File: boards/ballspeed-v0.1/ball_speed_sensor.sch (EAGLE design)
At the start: 7 parts, among them U1 MPM3620GQV-P

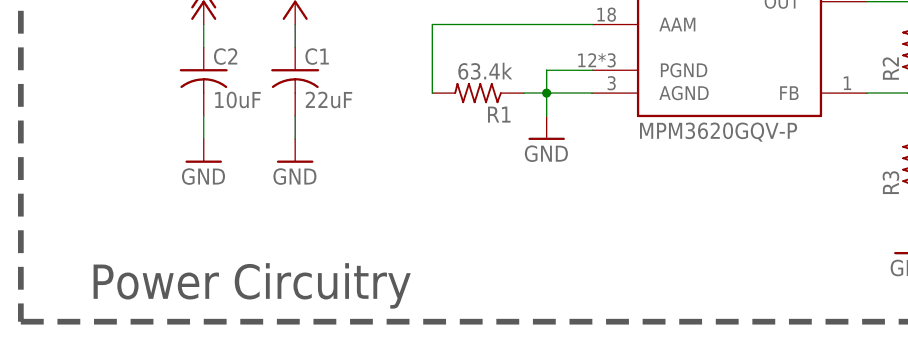
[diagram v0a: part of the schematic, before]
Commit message: Update ball_speed_sensor.sch
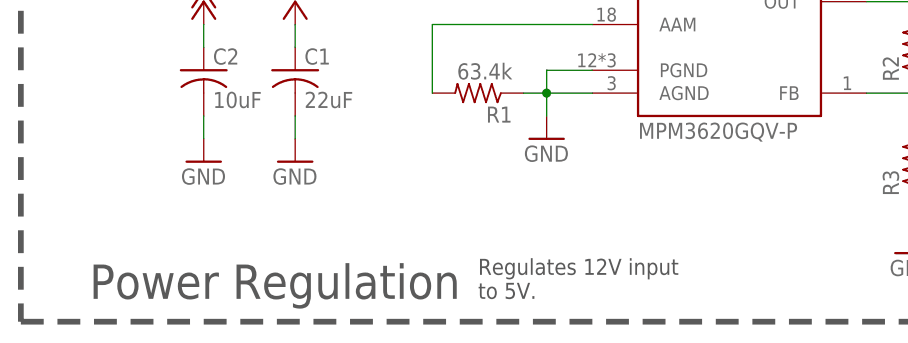
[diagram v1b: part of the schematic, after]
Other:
- note added: "Power Regulation"
- note added: "Regulates 12V input to 5V."
- note removed: "Power Circuitry"
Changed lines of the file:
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@@
 <wire x1="86.36" y1="231.14" x2="-25.4" y2="231.14" width="0.635" layer="97" style="longdash"/>
 <wire x1="-25.4" y1="231.14" x2="-25.4" y2="160.02" width="0.635" layer="97" style="longdash"/>
-<text x="-17.78" y="162.56" size="3.81" layer="97">Power Circuitry</text>
+<text x="-17.78" y="162.56" size="3.81" layer="97">Power Regulation</text>
+<text x="25.4" y="162.56" size="1.778" layer="97">Regulates 12V input
+to 5V.</text>
 </plain>
 <instances>
@@
 </drawing>
 <compatibility>
+<note version="6.3" minversion="6.2.2" severity="warning">
+Since Version 6.2.2 text objects can contain more than one line,
+which will not be processed correctly with this version.
+</note>
 <note version="8.2" severity="warning">
 Since Version 8.2, EAGLE supports online libraries. The ids
